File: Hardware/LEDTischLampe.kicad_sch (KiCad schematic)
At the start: 40 parts, among them J1 Conn_01x02_Socket, J2 USB_C_Receptacle_USB2.0_14P, J3 Conn_02x03_Counter_Clockwise, SW1 Reset, SW2 User, U1 ESP32-C3-WROOM-02, U7 RY8310

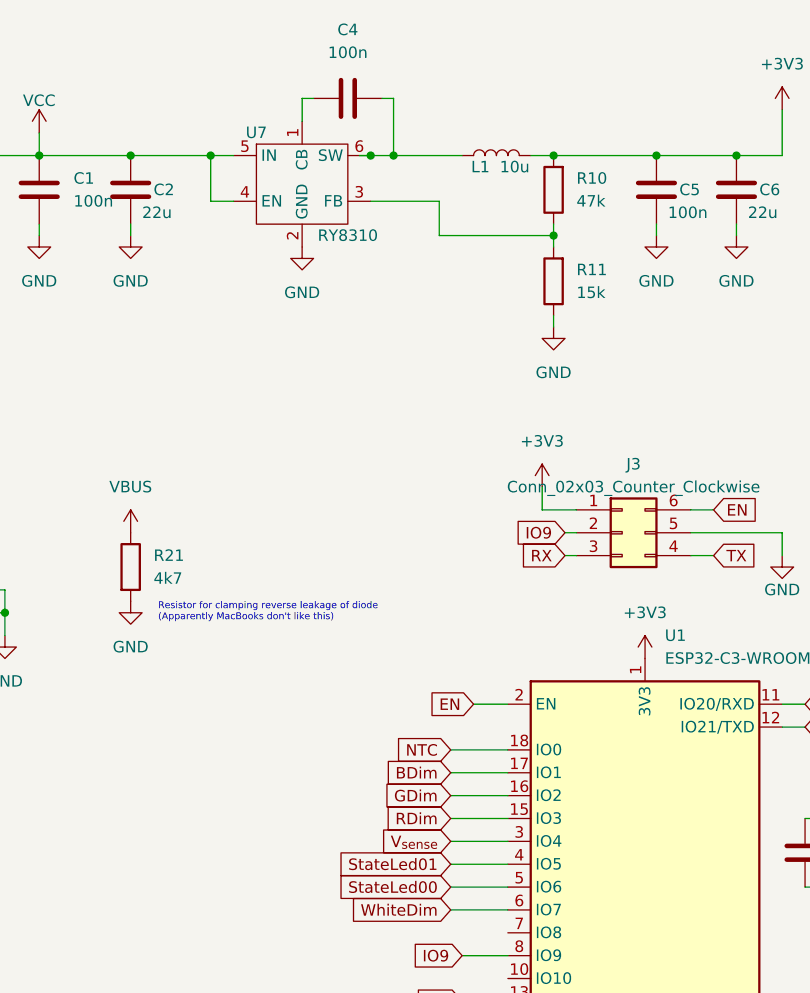
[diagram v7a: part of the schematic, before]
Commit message: update RGB mapping in KiCad
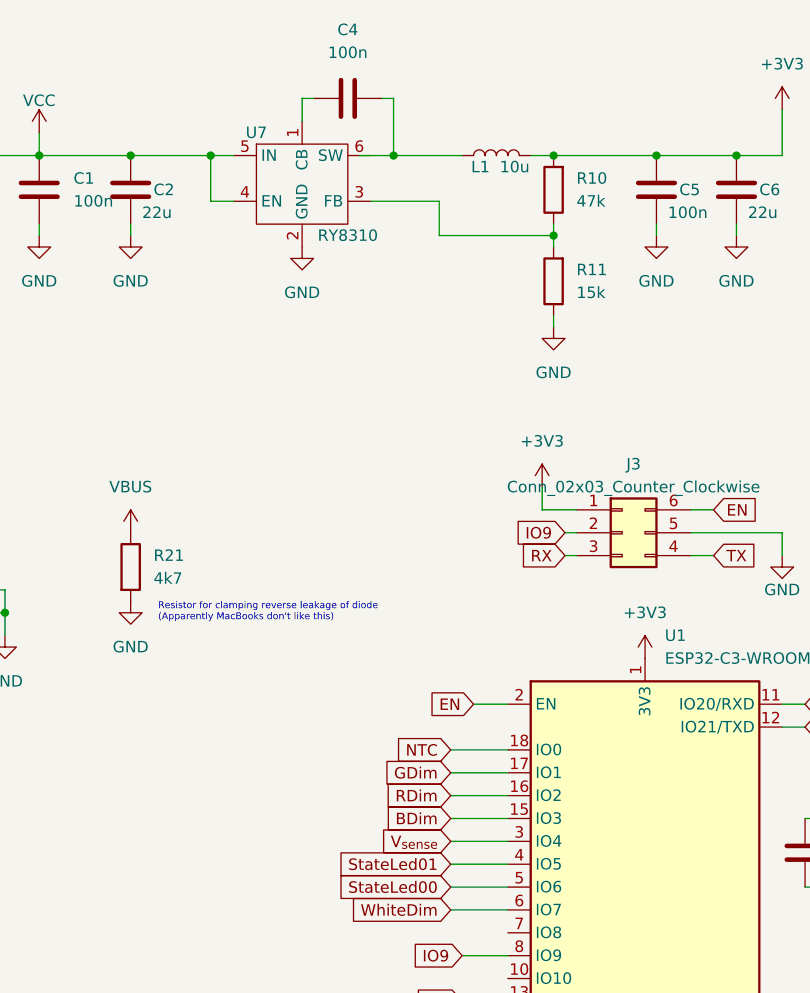
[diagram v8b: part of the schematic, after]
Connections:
- net BDim: now also U1.15 (IO3); no longer U1.17 (IO1)
- net GDim: now also U1.17 (IO1); no longer U1.16 (IO2)
- net RDim: now also U1.16 (IO2); no longer U1.15 (IO3)
- net at C4.2, L1.1: no longer U7.6 (SW)
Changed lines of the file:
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@@
-	)
-	(junction
-		(at 105.41 35.56)
-		(diameter 0)
-		(color 0 0 0 0)
 	)
 	(junction
@@
 	(wire
 		(pts
-			(xy 105.41 35.56) (xy 107.95 35.56)
+			(xy 104.14 35.56) (xy 107.95 35.56)
 		)
 		(stroke
@@
 		(pts
 			(xy 57.15 78.74) (xy 55.88 78.74)
-		)
-		(stroke
-			(width 0)
-			(type default)
-		)
-	)
-	(wire
-		(pts
-			(xy 104.14 35.56) (xy 105.41 35.56)
 		)
 		(stroke
@@
 		)
 	)
-	(global_label "RDim"
-		(shape input)
-		(at 114.3 109.22 180)
+	(global_label "StateLed00"
+		(shape input)
+		(at 114.3 116.84 180)
 		(fields_autoplaced yes)
 		(effects
@@
 		)
 		(property "Intersheetrefs" "${INTERSHEET_REFS}"
-			(at 106.4767 109.22 0)
+			(at 100.7316 116.84 0)
 			(effects
 				(font
@@
 		)
 	)
-	(global_label "StateLed00"
-		(shape input)
-		(at 114.3 116.84 180)
+	(global_label "EN"
+		(shape input)
+		(at 116.84 96.52 180)
 		(fields_autoplaced yes)
 		(effects
@@
 		)
 		(property "Intersheetrefs" "${INTERSHEET_REFS}"
-			(at 100.7316 116.84 0)
+			(at 111.3753 96.52 0)
 			(effects
 				(font
@@
 		)
 	)
-	(global_label "EN"
-		(shape input)
-		(at 116.84 96.52 180)
+	(global_label "RX"
+		(shape input)
+		(at 127 80.01 180)
 		(fields_autoplaced yes)
 		(effects
@@
 		)
 		(property "Intersheetrefs" "${INTERSHEET_REFS}"
-			(at 111.3753 96.52 0)
+			(at 121.5353 80.01 0)
 			(effects
 				(font
@@
 		)
 	)
-	(global_label "RX"
-		(shape input)
-		(at 127 80.01 180)
+	(global_label "DN"
+		(shape input)
+		(at 54.61 93.98 0)
+		(fields_autoplaced yes)
+		(effects
+			(font
+				(size 1.27 1.27)
+			)
+			(justify left)
+		)
+		(property "Intersheetrefs" "${INTERSHEET_REFS}"
+			(at 60.1957 93.98 0)
+			(effects
+				(font
+					(size 1.27 1.27)
+				)
+				(justify left)
+				(hide yes)
+			)
+		)
+	)
+	(global_label "WhiteDim"
+		(shape input)
+		(at 114.3 119.38 180)
 		(fields_autoplaced yes)
 		(effects
@@
 		)
 		(property "Intersheetrefs" "${INTERSHEET_REFS}"
-			(at 121.5353 80.01 0)
+			(at 102.7272 119.38 0)
 			(effects
 				(font
@@
 		)
 	)
-	(global_label "DN"
-		(shape input)
-		(at 54.61 93.98 0)
+	(global_label "IO9"
+		(shape input)
+		(at 127 77.47 180)
+		(fields_autoplaced yes)
+		(effects
+			(font
+				(size 1.27 1.27)
+			)
+			(justify right)
+		)
+		(property "Intersheetrefs" "${INTERSHEET_REFS}"
+			(at 120.87 77.47 0)
+			(effects
+				(font
+					(size 1.27 1.27)
+				)
+				(justify right)
+				(hide yes)
+			)
+		)
+	)
+	(global_label "RDim"
+		(shape input)
+		(at 114.3 106.68 180)
+		(fields_autoplaced yes)
+		(effects
+			(font
+				(size 1.27 1.27)
+			)
+			(justify right)
+		)
+		(property "Intersheetrefs" "${INTERSHEET_REFS}"
+			(at 106.4767 106.68 0)
+			(effects
+				(font
+					(size 1.27 1.27)
+				)
+				(justify right)
+				(hide yes)
+			)
+		)
+	)
+	(global_label "StateLed00"
+		(shape input)
+		(at 99.06 181.61 270)
+		(fields_autoplaced yes)
+		(effects
+			(font
+				(size 1.27 1.27)
+			)
+			(justify right)
+		)
+		(property "Intersheetrefs" "${INTERSHEET_REFS}"
+			(at 99.06 195.1784 90)
+			(effects
+				(font
+					(size 1.27 1.27)
+				)
+				(justify right)
+				(hide yes)
+			)
+		)
+	)
+	(global_label "NTC"
+		(shape input)
+		(at 143.51 176.53 0)
 		(fields_autoplaced yes)
 		(effects
@@
 		)
 		(property "Intersheetrefs" "${INTERSHEET_REFS}"
-			(at 60.1957 93.98 0)
+			(at 150.0633 176.53 0)
 			(effects
 				(font
@@
 		)
 	)
-	(global_label "WhiteDim"
-		(shape input)
-		(at 114.3 119.38 180)
+	(global_label "GDim"
+		(shape input)
+		(at 114.3 104.14 180)
 		(fields_autoplaced yes)
 		(effects
@@
 		)
 		(property "Intersheetrefs" "${INTERSHEET_REFS}"
-			(at 102.7272 119.38 0)
+			(at 106.4767 104.14 0)
 			(effects
 				(font
@@
 		)
 	)
-	(global_label "IO9"
-		(shape input)
-		(at 127 77.47 180)
+	(global_label "DP"
+		(shape input)
+		(at 115.57 132.08 180)
 		(fields_autoplaced yes)
 		(effects
@@
 		)
 		(property "Intersheetrefs" "${INTERSHEET_REFS}"
-			(at 120.87 77.47 0)
+			(at 110.0448 132.08 0)
 			(effects
 				(font
@@
 		)
 	)
-	(global_label "BDim"
-		(shape input)
-		(at 114.3 104.14 180)
-		(fields_autoplaced yes)
-		(effects
-			(font
-				(size 1.27 1.27)
-			)
-			(justify right)
-		)
-		(property "Intersheetrefs" "${INTERSHEET_REFS}"
-			(at 106.4767 104.14 0)
-			(effects
-				(font
-					(size 1.27 1.27)
-				)
-				(justify right)
-				(hide yes)
-			)
-		)
-	)
-	(global_label "StateLed00"
-		(shape input)
-		(at 99.06 181.61 270)
-		(fields_autoplaced yes)
-		(effects
-			(font
-				(size 1.27 1.27)
-			)
-			(justify right)
-		)
-		(property "Intersheetrefs" "${INTERSHEET_REFS}"
-			(at 99.06 195.1784 90)
-			(effects
-				(font
-					(size 1.27 1.27)
-				)
-				(justify right)
-				(hide yes)
-			)
-		)
-	)
-	(global_label "NTC"
-		(shape input)
-		(at 143.51 176.53 0)
+	(global_label "EN"
+		(shape input)
+		(at 143.51 74.93 0)
 		(fields_autoplaced yes)
 		(effects
@@
 		)
 		(property "Intersheetrefs" "${INTERSHEET_REFS}"
-			(at 150.0633 176.53 0)
+			(at 148.9747 74.93 0)
 			(effects
 				(font
@@
 	(global_label "DP"
 		(shape input)
-		(at 115.57 132.08 180)
-		(fields_autoplaced yes)
-		(effects
-			(font
-				(size 1.27 1.27)
-			)
-			(justify right)
-		)
-		(property "Intersheetrefs" "${INTERSHEET_REFS}"
-			(at 110.0448 132.08 0)
-			(effects
-				(font
-					(size 1.27 1.27)
-				)
-				(justify right)
-				(hide yes)
-			)
-		)
-	)
-	(global_label "EN"
-		(shape input)
-		(at 143.51 74.93 0)
+		(at 54.61 99.06 0)
 		(fields_autoplaced yes)
 		(effects
@@
 		)
 		(property "Intersheetrefs" "${INTERSHEET_REFS}"
-			(at 148.9747 74.93 0)
+			(at 60.1352 99.06 0)
 			(effects
 				(font
@@
 		)
 	)
-	(global_label "DP"
-		(shape input)
-		(at 54.61 99.06 0)
-		(fields_autoplaced yes)
-		(effects
-			(font
-				(size 1.27 1.27)
-			)
-			(justify left)
-		)
-		(property "Intersheetrefs" "${INTERSHEET_REFS}"
-			(at 60.1352 99.06 0)
-			(effects
-				(font
-					(size 1.27 1.27)
-				)
-				(justify left)
-				(hide yes)
-			)
-		)
-	)
-	(global_label "GDim"
-		(shape input)
-		(at 114.3 106.68 180)
+	(global_label "BDim"
+		(shape input)
+		(at 114.3 109.22 180)
 		(fields_autoplaced yes)
 		(effects
@@
 		)
 		(property "Intersheetrefs" "${INTERSHEET_REFS}"
-			(at 106.4767 106.68 0)
-			(effects
-				(font
+			(at 106.4767 109.22 0)
+			(effects
+				(font
